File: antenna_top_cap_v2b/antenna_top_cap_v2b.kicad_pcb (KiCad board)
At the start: 4 copper layers, 100 x 100 mm, 59 parts, among them J1 DEBUG, J10 WDT Disable Jumper, J11 DF11-4DP-2DSA, J12 USB_C_Receptacle_USB2.0_16P, J13 DNP, J2 Battery Charge Bypass, J3 FC Reset Jumper, J4 FC USB Bootselect Jumper, J5 Conn_Coaxial, J8 USB_C_Receptacle_USB2.0_16P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

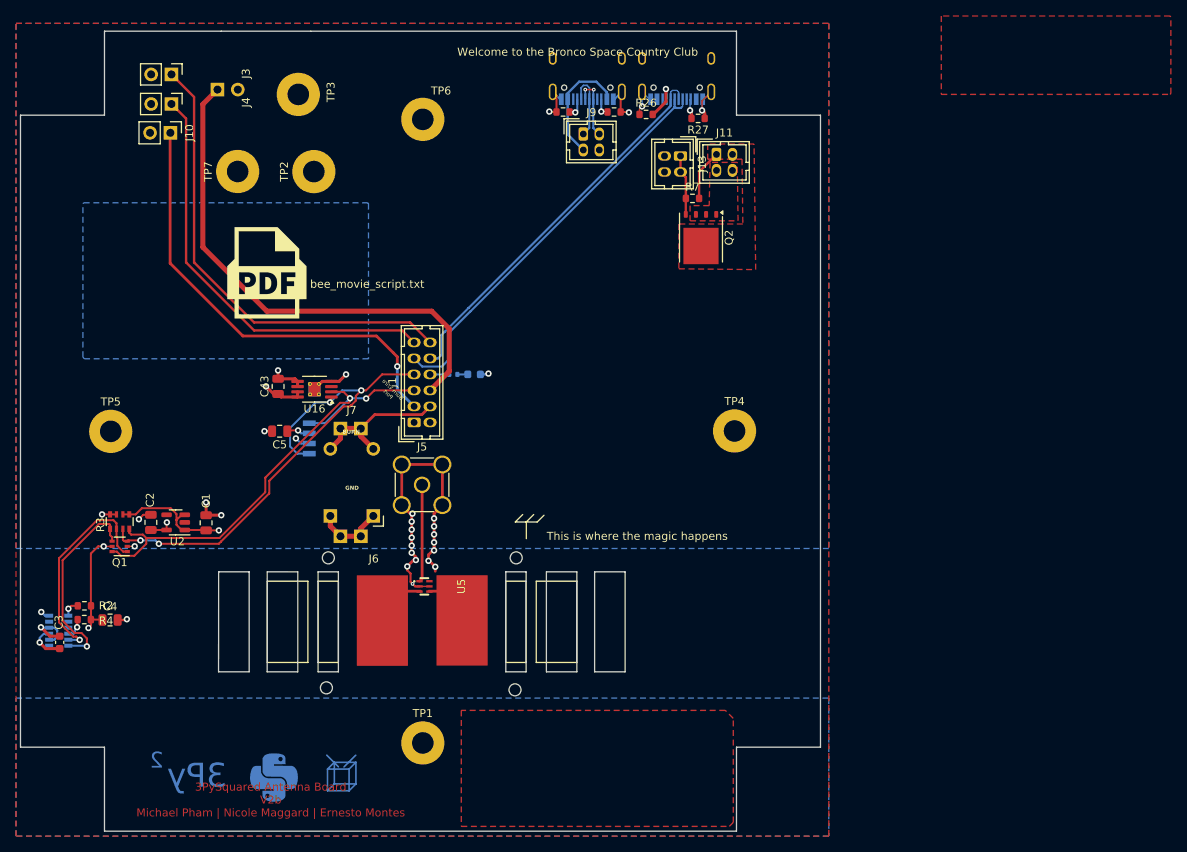
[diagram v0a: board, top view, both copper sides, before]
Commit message: V2b: Switched From VEML7700 to VEML61
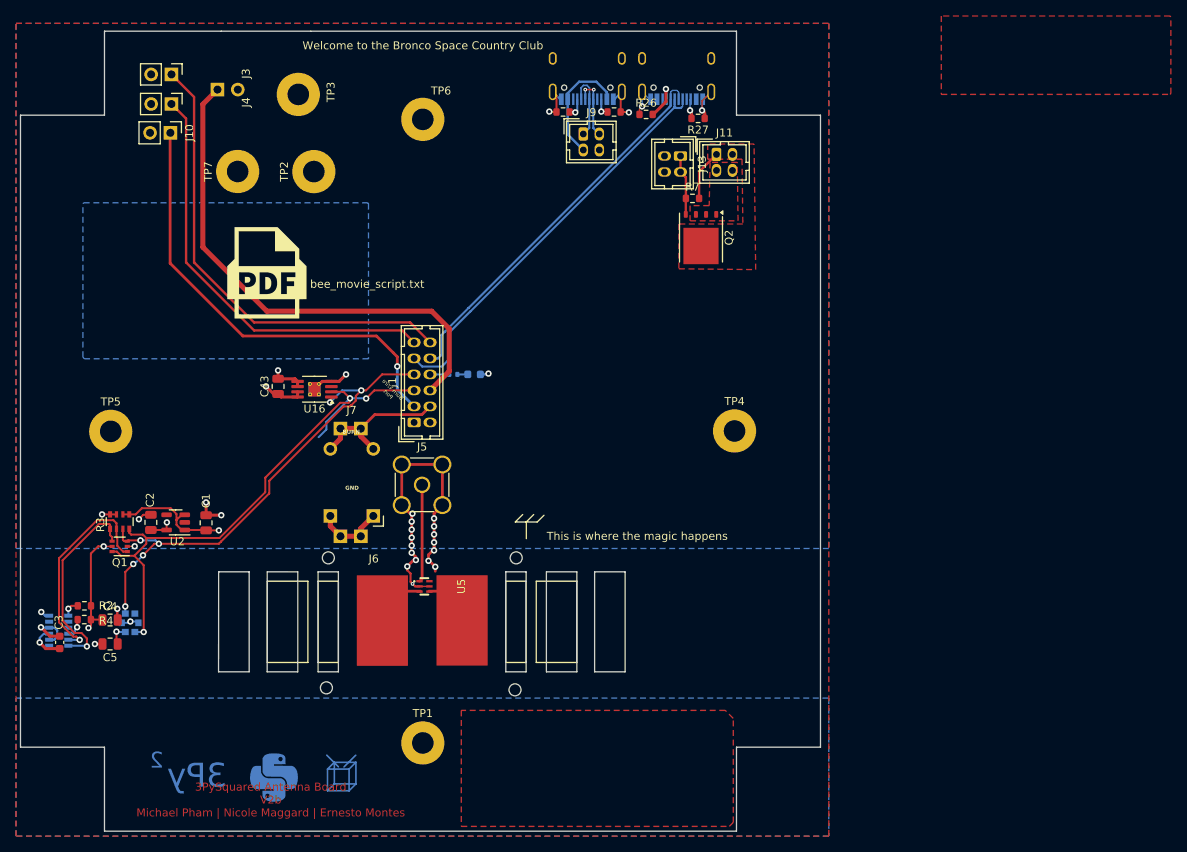
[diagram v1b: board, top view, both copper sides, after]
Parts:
- removed U4: VEML7700, VEML7700-TT:XDCR_VEML7700-TT
- added U3: VEML6031X00, easyeda2kicad:SENSOR-SMD_VEML6031X00, B.Cu at (129.2, 136.2)
- G***: moved to F.Cu
- moved C5 34.0 mm to (126.7, 138.8)
- moved G*** 7.98 mm to (186.4, 92.1), turned to 0 degrees
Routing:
- net SCL0: track 60.2 -> 71.4 mm, vias 2 -> 3
- net GND: track 94.4 -> 94.9 mm
- net SDA0: track 64.8 -> 64.6 mm, vias 4 -> 7

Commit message: As ORdered For V3 Pro
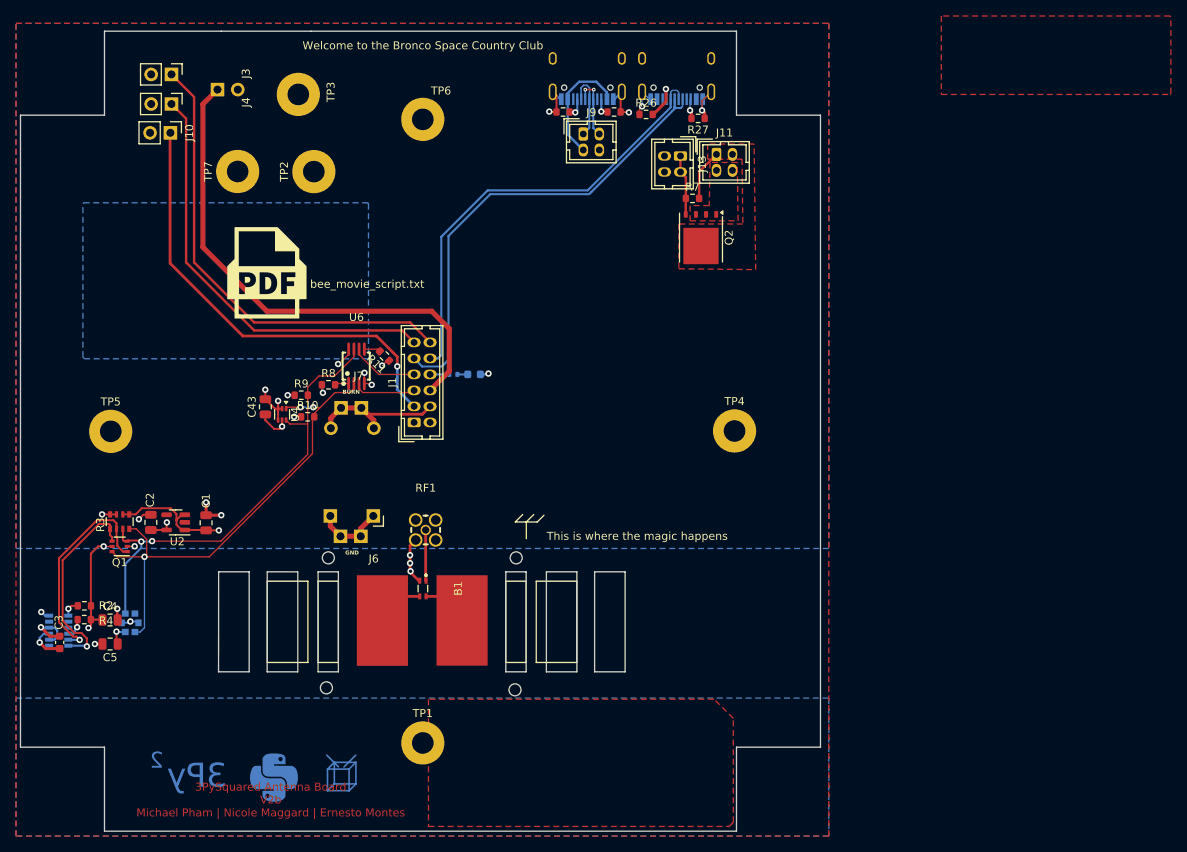
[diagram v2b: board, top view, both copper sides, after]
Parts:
- removed J5: Conn_Coaxial, Connector_Coaxial:SMA_Amphenol_901-144_Vertical
- removed U16: MCP9808T-E/MS, Package_SO:MSOP-8-1EP_3x3mm_P0.65mm_EP1.5x1.8mm_ThermalVias
- removed U5: HHM1591D1, easyeda2kicad:XFMR-SMD_HHM1591D1
- added B1: ATB2012-50011-T000, easyeda2kicad:XFMR-SMD_ATB2012-50011-T000, F.Cu at (165.8, 131.9)
- added G***: LOGO, LOGO, B.Cu at (187.0, 93.9)
- added R10: 10k, Resistor_SMD:R_0603_1608Metric, F.Cu at (151.4, 110.4)
- added R11: 10k, Resistor_SMD:R_0603_1608Metric, F.Cu at (161.0, 102.8)
- added R8: 10k, Resistor_SMD:R_0603_1608Metric, F.Cu at (154.0, 106.4)
- added R9: 10k, Resistor_SMD:R_0603_1608Metric, F.Cu at (150.6, 107.7)
- added RF1: KH-MMCX-Z, easyeda2kicad:MMCX-TH_KH-MMCX-Z, F.Cu at (166.2, 124.6)
- added U4: TMP112xxDRL, Package_TO_SOT_SMD:SOT-563, F.Cu at (148.2, 110.1)
- added U6: TCA4311ADGKR, easyeda2kicad:MSOP-8_L3.0-W3.0-P0.65-LS5.0-BL, F.Cu at (157.5, 104.1)
- moved G*** 44.2 mm to (186.8, 113.4)
- moved C43 3.01 mm to (146.2, 109.2)
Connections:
- Q1 pad 3: SDA0 -> SDA1
- Q1 pad 6: SCL0 -> SCL1
- R3 pad 7: SDA0 -> SDA1
- R3 pad 8: SCL0 -> SCL1
- U3 pad 2: SDA0 -> SDA1
- U3 pad 5: SCL0 -> SCL1
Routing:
- net SCL0: track 71.4 -> 7.84 mm, vias 3 -> 0
- net SCL1: track 0.00 -> 62.3 mm, vias 0 -> 3
- net SDA1: track 0.00 -> 58.6 mm, vias 0 -> 2
- net SDA0: track 64.6 -> 8.57 mm, vias 7 -> 0
- net GND: track 94.9 -> 61.8 mm, vias 31 -> 20
- net Net-(J5-In): track 12.2 -> 0.00 mm
- net USB_D-: track 48.4 -> 55.7 mm
- net USB_D+: track 51.4 -> 58.7 mm
- net Net-(B1-U.P.50): track 0.00 -> 6.36 mm
- net +3V3: track 25.8 -> 31.3 mm, vias 3 -> 8
- net Net-(U6-READY): track 0.00 -> 2.05 mm
- net Net-(U6-EN): track 0.00 -> 1.76 mm
- net Net-(J6-tape_1): track 5.03 -> 6.22 mm
- net Net-(B1-B.P.50): track 4.72 -> 5.74 mm
- removed copper zone on In1.Cu, net Dir_Chrg_In
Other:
- board text added: "PROVES on the Ocean F′ on Mars Zephyr on the Wind PROVES, F′, and Zephyr at Tanagra The Beast at Tanagra PROVES, F′, and Zephyr on the Wind and Ocean"
- board text removed: "3PySquared Antenna Board V2 Michael Pham | Nicole Maggard | Ernesto Montes"
- board text removed: "Burn Wire Port"
